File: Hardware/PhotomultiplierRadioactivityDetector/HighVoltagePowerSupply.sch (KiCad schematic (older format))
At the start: 0 parts

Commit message: draft of hw power supply
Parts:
- added C10, C11, C12, C7: 100n, Capacitor_SMD:C_0805_2012Metric_Pad1.15x1.40mm_HandSolder, symbol Device:C
- added C13: C, Capacitor_THT:C_Disc_D8.0mm_W2.5mm_P5.00mm, symbol Device:C
- added C14, C15, C16, C17: 10n, Capacitor_THT:C_Disc_D11.0mm_W5.0mm_P7.50mm, symbol Device:C
- added C8, C9: 10n, Capacitor_SMD:C_0805_2012Metric_Pad1.15x1.40mm_HandSolder, symbol Device:C
- added D4: red, LED_SMD:LED_0805_2012Metric, symbol Device:LED
- added D5: D, symbol Device:D
- added Q3: Q_NMOS_GDS, Package_TO_SOT_THT:TO-220-3_Horizontal_TabDown, symbol Device:Q_NMOS_GDS
- added R16, R17, R18, R19: 10k, Resistor_SMD:R_0805_2012Metric_Pad1.15x1.40mm_HandSolder, symbol Device:R
- added R20, R21: 10k, Resistor_THT:R_Axial_DIN0411_L9.9mm_D3.6mm_P12.70mm_Horizontal, symbol Device:R
- added TP1: TestPoint, TestPoint:TestPoint_Loop_D2.60mm_Drill0.9mm_Beaded, symbol Connector:TestPoint
- added TR1: TRANSF1, symbol Transformer:TRANSF1
- added U4: LM3488, Package_SO:VSSOP-8_2.4x2.1mm_P0.5mm, symbol PhotomultiplierRadioactivityDetector:LM3488
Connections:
- new net: C9.2, Q3.3 (S), R19.1, U4.1 (Isen)
- new net: R17.1, U4.2 (COMP)
- new net: C13.1, R20.2, R21.1, U4.3 (FB)
- new net: Q3.1 (G), U4.6 (DR)
- new net: R18.1, U4.7 (FA/SYNC/SD)
- new net: Q3.2 (D), TR1.2
- new net: D4.1 (K), R16.1
- new net: C14.2, C15.2, C16.2, C17.2, D5.1 (K), R20.1, TP1.1
- new net: C8.2, R17.2
- new net: D5.2 (A), TR1.4
- new net GND: C10.2, C11.2, C12.2, C13.2, C14.1, C15.1, C16.1, C17.1, C7.1, C8.1, C9.1, R16.2, R18.2, R19.2, R21.2, TR1.3, U4.4 (AGND), U4.~ (PGND)
- new net VCC: C10.1, C11.1, C12.1, C7.2, D4.2 (A), TR1.1, U4.8 (Vin)
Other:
- note added: "Place C23 close to Vin.\nPlace C10-C12 close to T1."
- note added: "TODO element values."

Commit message: draft of amplifier
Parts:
- D5: footprint (none) -> Diode_SMD:D_MELF
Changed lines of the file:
@@
 $Descr A4 11693 8268
 encoding utf-8
-Sheet 3 5
+Sheet 3 6
 Title ""
 Date ""
@@
 F 0 "D5" H 7500 2483 50  0000 C CNN
 F 1 "D" H 7500 2574 50  0000 C CNN
-F 2 "" H 7500 2700 50  0001 C CNN
+F 2 "Diode_SMD:D_MELF" H 7500 2700 50  0001 C CNN
 F 3 "~" H 7500 2700 50  0001 C CNN
 	1    7500 2700

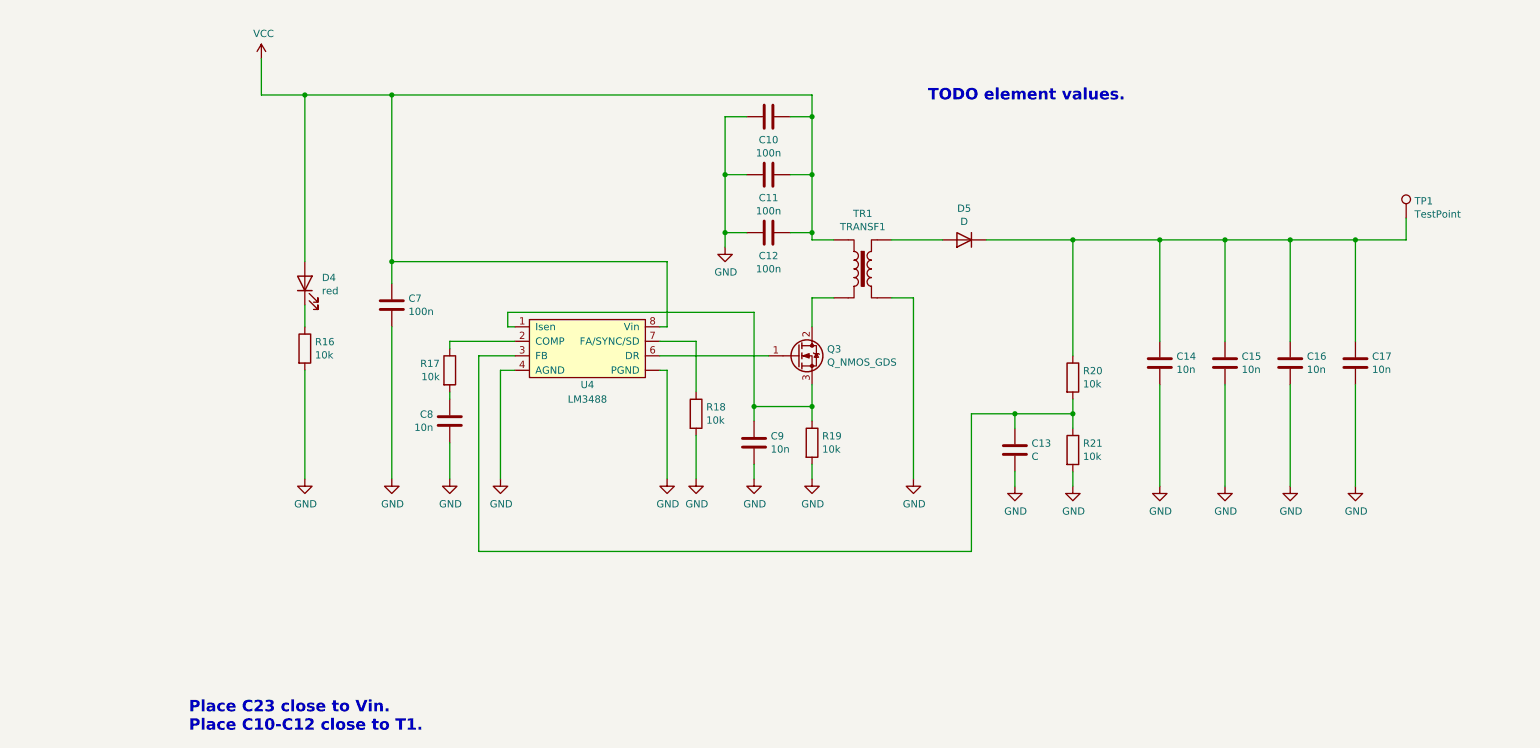
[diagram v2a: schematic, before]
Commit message: placement of components for tube driver
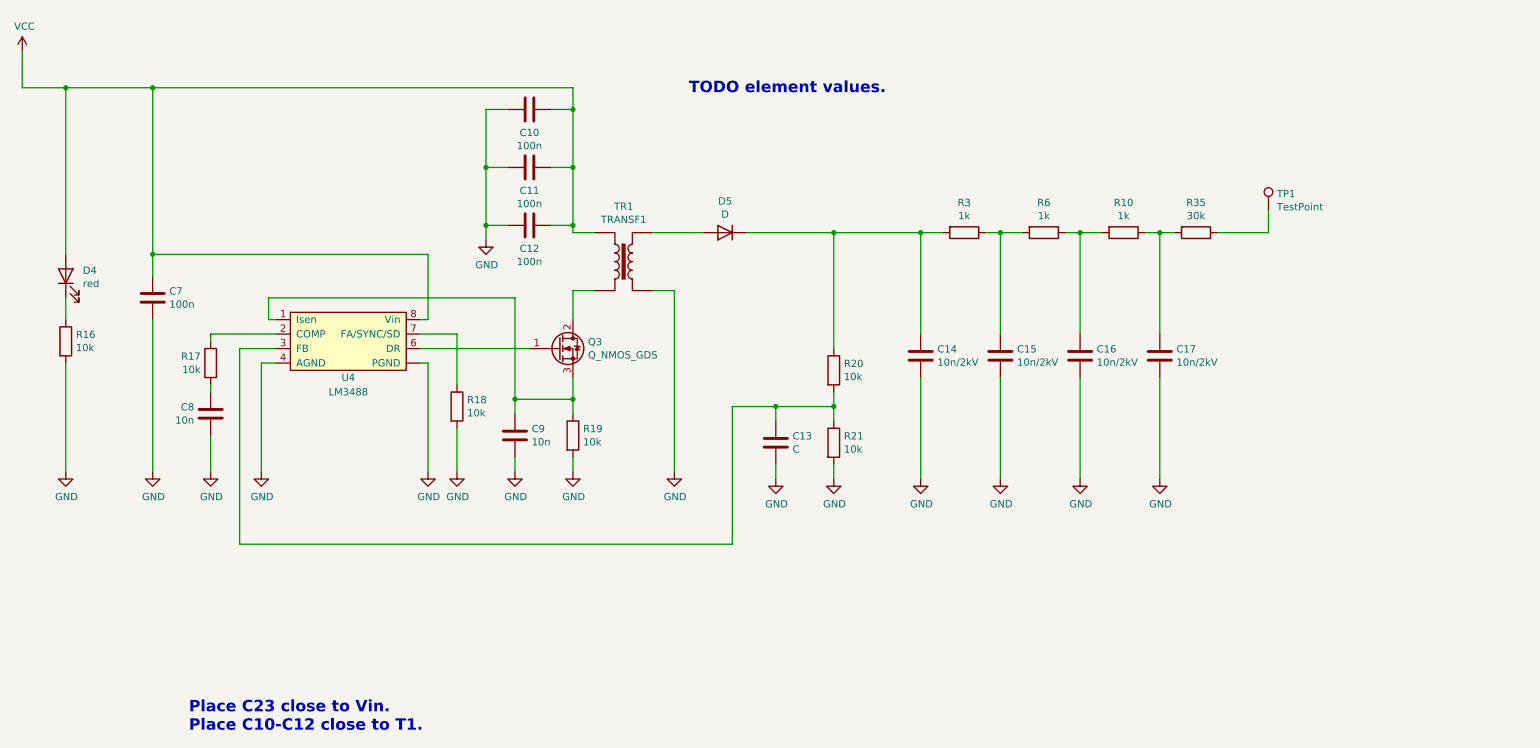
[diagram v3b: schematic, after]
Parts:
- added R10, R3, R6: 1k, Resistor_SMD:R_0805_2012Metric_Pad1.15x1.40mm_HandSolder, symbol Device:R
- added R35: 30k, Resistor_SMD:R_MELF_MMB-0207, symbol Device:R
- C14, C15, C16, C17: value 10n -> 10n/2kV
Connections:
- new net: R35.1, TP1.1
- new net: C14.2, D5.1 (K), R20.1, R3.2
- new net: C15.2, R3.1, R6.2
- new net: C16.2, R10.2, R6.1
- new net: C17.2, R10.1, R35.2
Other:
- moved on the sheet: C10, C11, C12, C13, C14, C15, C16, C17, C7, C8, C9, D4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

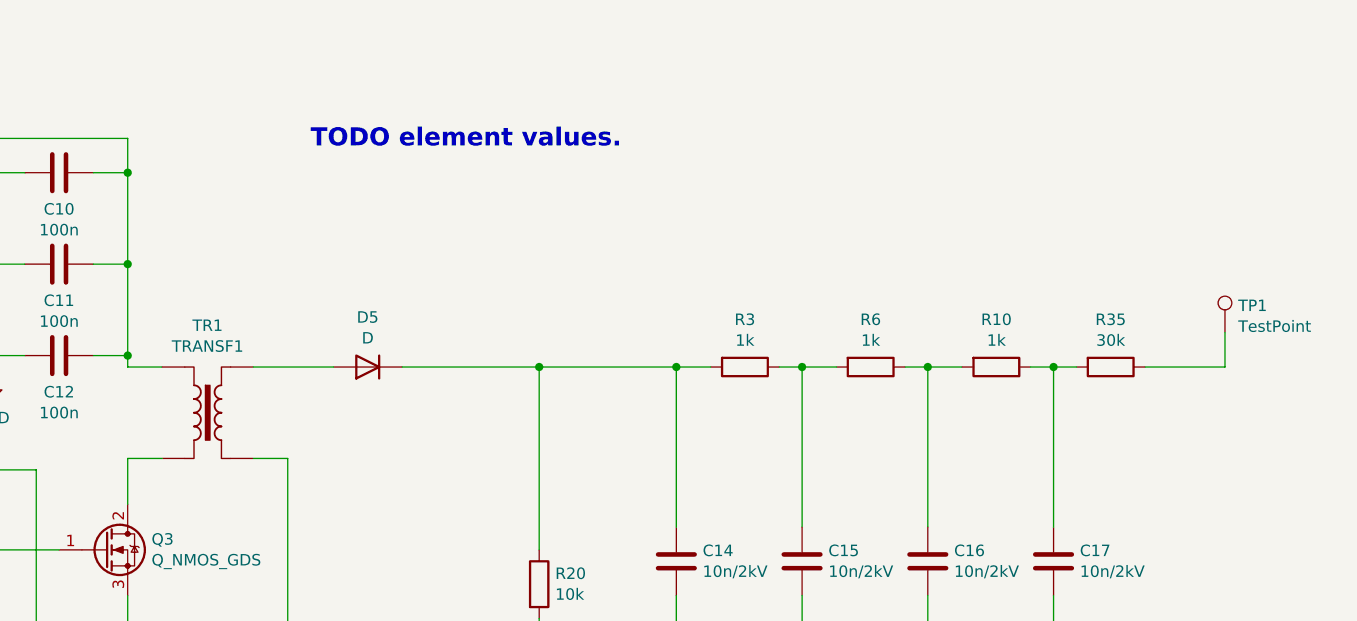
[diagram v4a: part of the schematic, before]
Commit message: add element,, footprint and 3d model for transformer
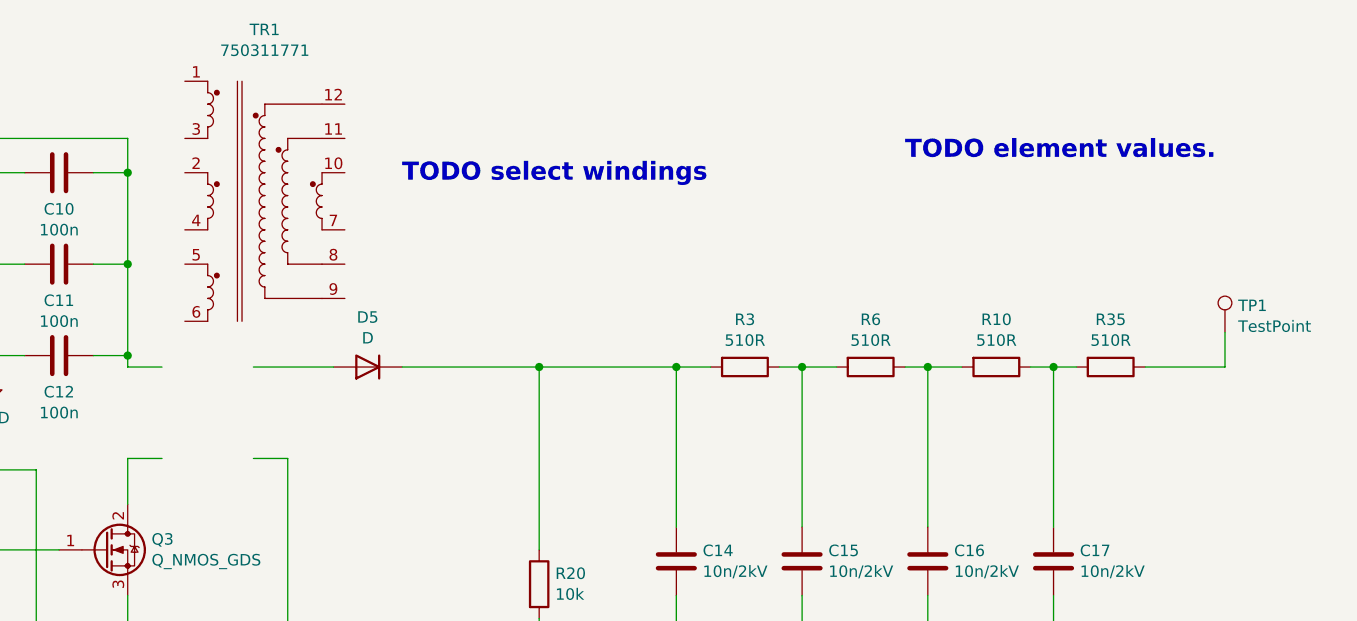
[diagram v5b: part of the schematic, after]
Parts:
- removed TR1: TRANSF1, symbol Transformer:TRANSF1
- added TR1: 750311771, PhotomultiplierRadioactivityDetector:750311771, symbol PhotomultiplierRadioactivityDetector:750311771
- R10, R3, R6: value 1k -> 510R
- R35: value 30k -> 510R
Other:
- note added: "TODO select windings"
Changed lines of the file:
@@
 	-1   0    0    1
-$EndComp
-$Comp
-L Transformer:TRANSF1 TR1
-U 1 1 5EDE08EB
-P 5150 2850
-F 0 "TR1" H 5150 3231 50  0000 C CNN
-F 1 "TRANSF1" H 5150 3140 50  0000 C CNN
-F 2 "" H 5150 2850 50  0001 C CNN
-F 3 "" H 5150 2850 50  0001 C CNN
-	1    5150 2850
-	1    0    0    -1
 $EndComp
 Wire Wire Line
@@
 Wire Wire Line
 	1300 1650 1300 2800
-Text Notes 5600 1700 0    79   ~ 16
+Text Notes 8200 1750 0    79   ~ 16
 TODO element values.
 $Comp
@@
 AR Path="/5EDA5628/5EE6CD60" Ref="R3"  Part="1"
 F 0 "R3" V 7293 2650 50  0000 C CNN
-F 1 "1k" V 7384 2650 50  0000 C CNN
+F 1 "510R" V 7384 2650 50  0000 C CNN
 F 2 "Resistor_SMD:R_0805_2012Metric_Pad1.15x1.40mm_HandSolder" V 7430 2650 50  0001 C CNN
 F 3 "~" H 7500 2650 50  0001 C CNN
@@
 AR Path="/5EDA5628/5EE7CEDA" Ref="R6"  Part="1"
 F 0 "R6" V 7843 2650 50  0000 C CNN
-F 1 "1k" V 7934 2650 50  0000 C CNN
+F 1 "510R" V 7934 2650 50  0000 C CNN
 F 2 "Resistor_SMD:R_0805_2012Metric_Pad1.15x1.40mm_HandSolder" V 7980 2650 50  0001 C CNN
 F 3 "~" H 8050 2650 50  0001 C CNN
@@
 AR Path="/5EDA5628/5EE7D17F" Ref="R10"  Part="1"
 F 0 "R10" V 8393 2650 50  0000 C CNN
-F 1 "1k" V 8484 2650 50  0000 C CNN
+F 1 "510R" V 8484 2650 50  0000 C CNN
 F 2 "Resistor_SMD:R_0805_2012Metric_Pad1.15x1.40mm_HandSolder" V 8530 2650 50  0001 C CNN
 F 3 "~" H 8600 2650 50  0001 C CNN
@@
 AR Path="/5EDA5628/5EEA3B44" Ref="R35"  Part="1"
 F 0 "R35" V 8893 2650 50  0000 C CNN
-F 1 "30k" V 8984 2650 50  0000 C CNN
+F 1 "510R" V 8984 2650 50  0000 C CNN
 F 2 "Resistor_SMD:R_MELF_MMB-0207" V 9030 2650 50  0001 C CNN
 F 3 "~" H 9100 2650 50  0001 C CNN
@@
 Wire Wire Line
 	9250 2650 9600 2650
+$Comp
+L PhotomultiplierRadioactivityDetector:750311771 TR1
+U 1 1 5EF92A84
+P 5300 1350
+F 0 "TR1" H 5400 1525 50  0000 C CNN
+F 1 "750311771" H 5400 1434 50  0000 C CNN
+F 2 "PhotomultiplierRadioactivityDetector:750311771" H 5300 1500 50  0001 C CNN
+F 3 "http://www.farnell.com/datasheets/1337718.pdf?_ga=2.65563566.1225228608.1593261089-1855792729.1592068583" H 5300 1500 50  0001 C CNN
+	1    5300 1350
+	1    0    0    -1
+$EndComp
+Text Notes 6000 1850 0    79   ~ 16
+TODO select windings
 $EndSCHEMATC

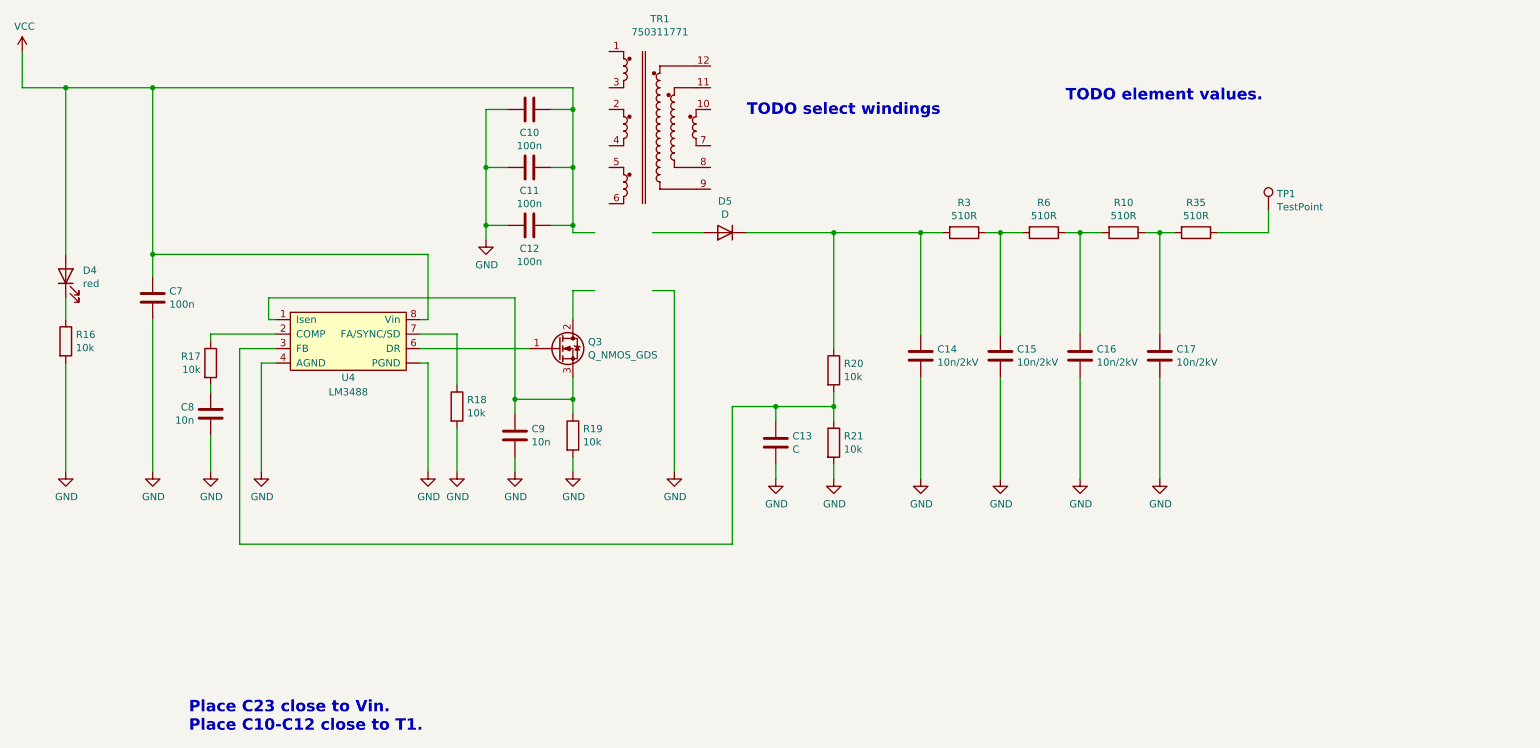
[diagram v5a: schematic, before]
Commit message: draft of simulation for hw power supply elements values
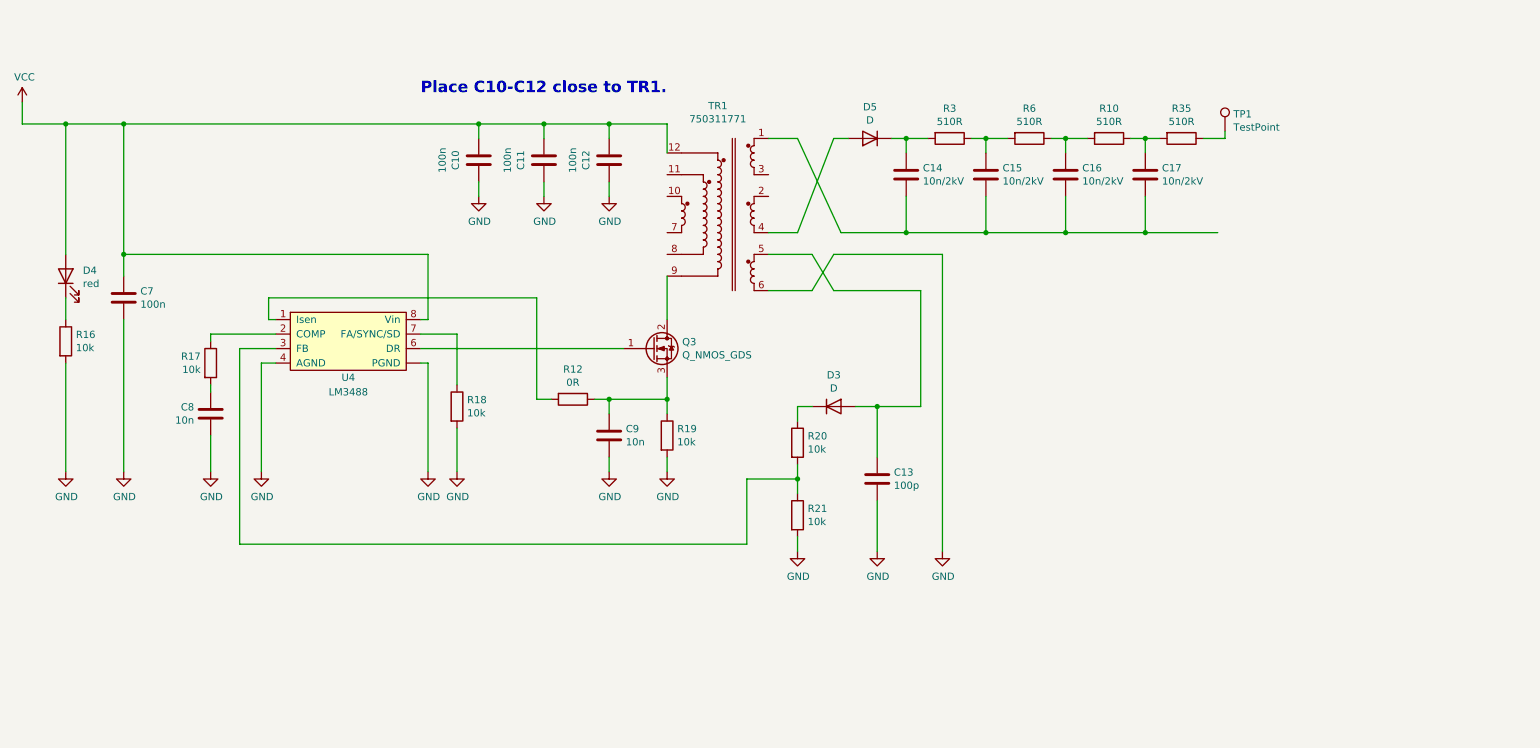
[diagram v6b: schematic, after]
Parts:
- added D3: D, Diode_SMD:D_MELF, symbol Device:D
- added R12: 0R, Resistor_SMD:R_0805_2012Metric_Pad1.15x1.40mm_HandSolder, symbol Device:R
- C13: value C -> 100p; footprint Capacitor_THT:C_Disc_D8.0mm_W2.5mm_P5.00mm -> Capacitor_SMD:C_0805_2012Metric_Pad1.15x1.40mm_HandSolder
- R10, R3, R6: footprint Resistor_SMD:R_0805_2012Metric_Pad1.15x1.40mm_HandSolder -> Resistor_SMD:R_MELF_MMB-0207
- R20, R21: footprint Resistor_THT:R_Axial_DIN0411_L9.9mm_D3.6mm_P12.70mm_Horizontal -> Resistor_SMD:R_MELF_MMB-0207
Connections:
- wire segments 85 -> 98
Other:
- note added: "Place C10-C12 close to TR1."
- note removed: "Place C23 close to Vin.\nPlace C10-C12 close to T1."
- note removed: "TODO element values."
- note removed: "TODO select windings"
- moved on the sheet: C10, C11, C12, C13, C14, C15, C16, C17, C7, C9, D5, Q3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
